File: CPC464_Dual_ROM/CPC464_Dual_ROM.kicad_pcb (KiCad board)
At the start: 2 copper layers, 21.7 x 40.3 mm, 4 parts, among them J1 Conn_01x02, U1 27256 Socket, U2 27512 ROM

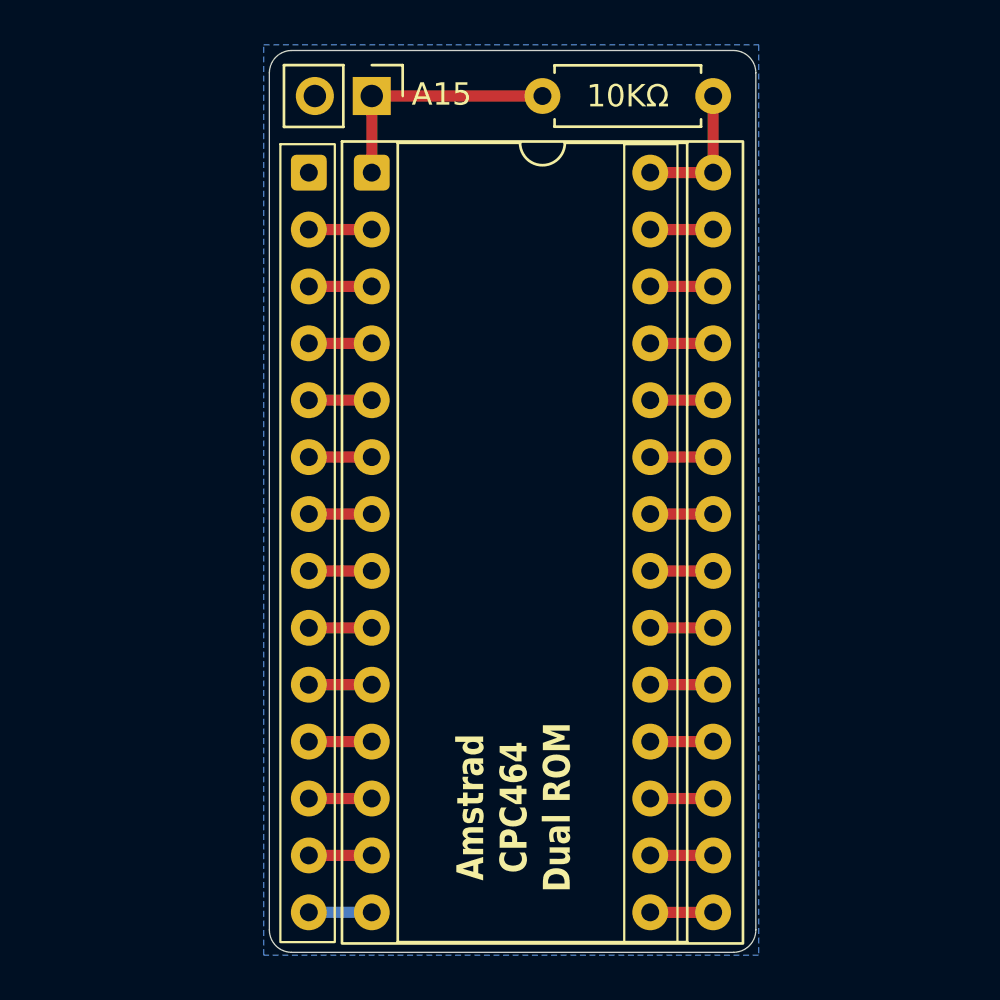
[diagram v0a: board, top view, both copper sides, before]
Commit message: Reorient PCB text
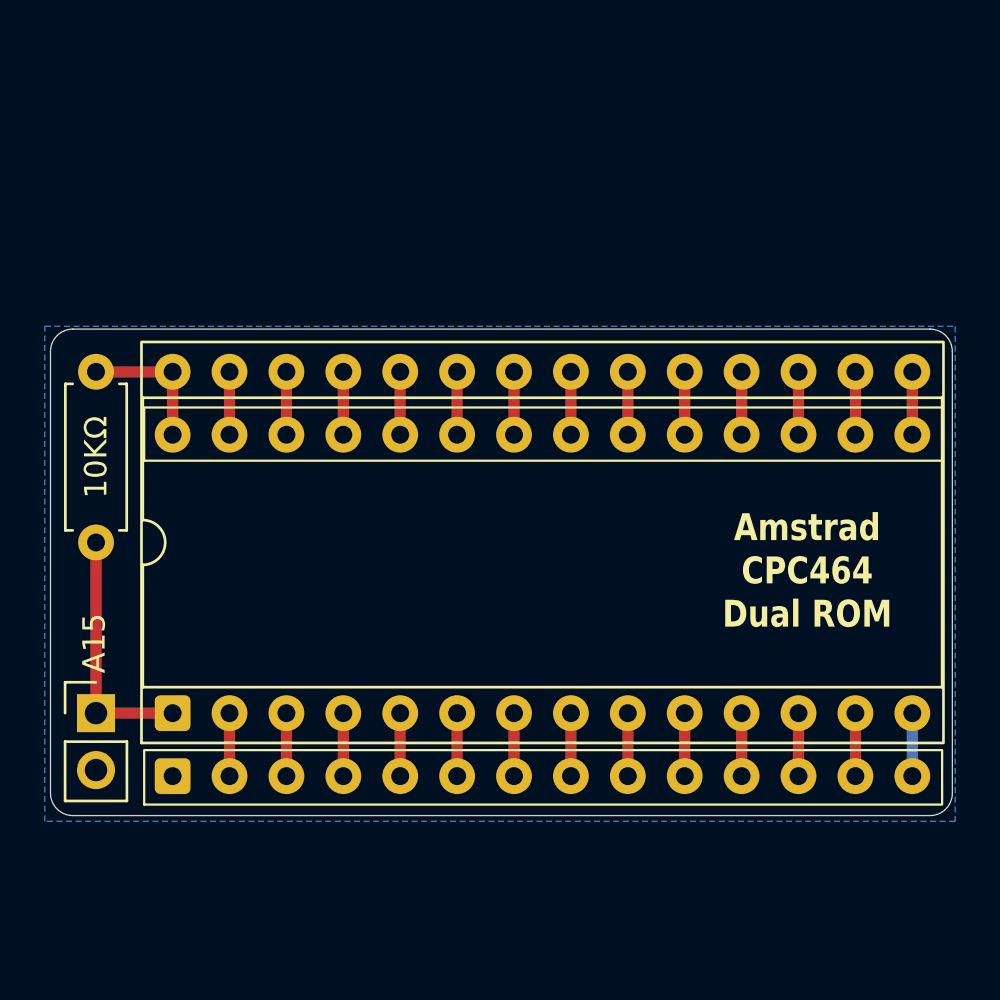
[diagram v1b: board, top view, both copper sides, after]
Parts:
- moved J1 30.2 mm to (94.4, 94.9), turned to 0 degrees
- moved R1 30.2 mm to (94.4, 79.6), turned to -90 degrees
- moved U1 27.6 mm to (97.8, 97.7), turned to 90 degrees
- moved U2 25.7 mm to (97.8, 94.9), turned to 90 degrees
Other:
- board size 21.7 x 40.3 mm -> 40.3 x 21.7 mm
